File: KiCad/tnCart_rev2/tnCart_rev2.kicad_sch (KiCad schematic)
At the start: 97 parts, among them CN1 MSX_Cartridge, J1 Conn_01x06_Pin, J2 ST-005-G, Q10 2SC2712, Q11 2SC2712, SW1 SW_DIP_x01, U1 TangNano20K, U10 TC74LCX163245FT, U20 TC74LCX163245FT, U30 TC74LCX163245FT, U40 74LVC1G139, U41 74LVC1G125, U60 LP2985-3.3, U70 LMV7219M5, U71 R-R, U80 LMV7219M5, U81 R-R, U90 LMV7219M5, U91 R-R

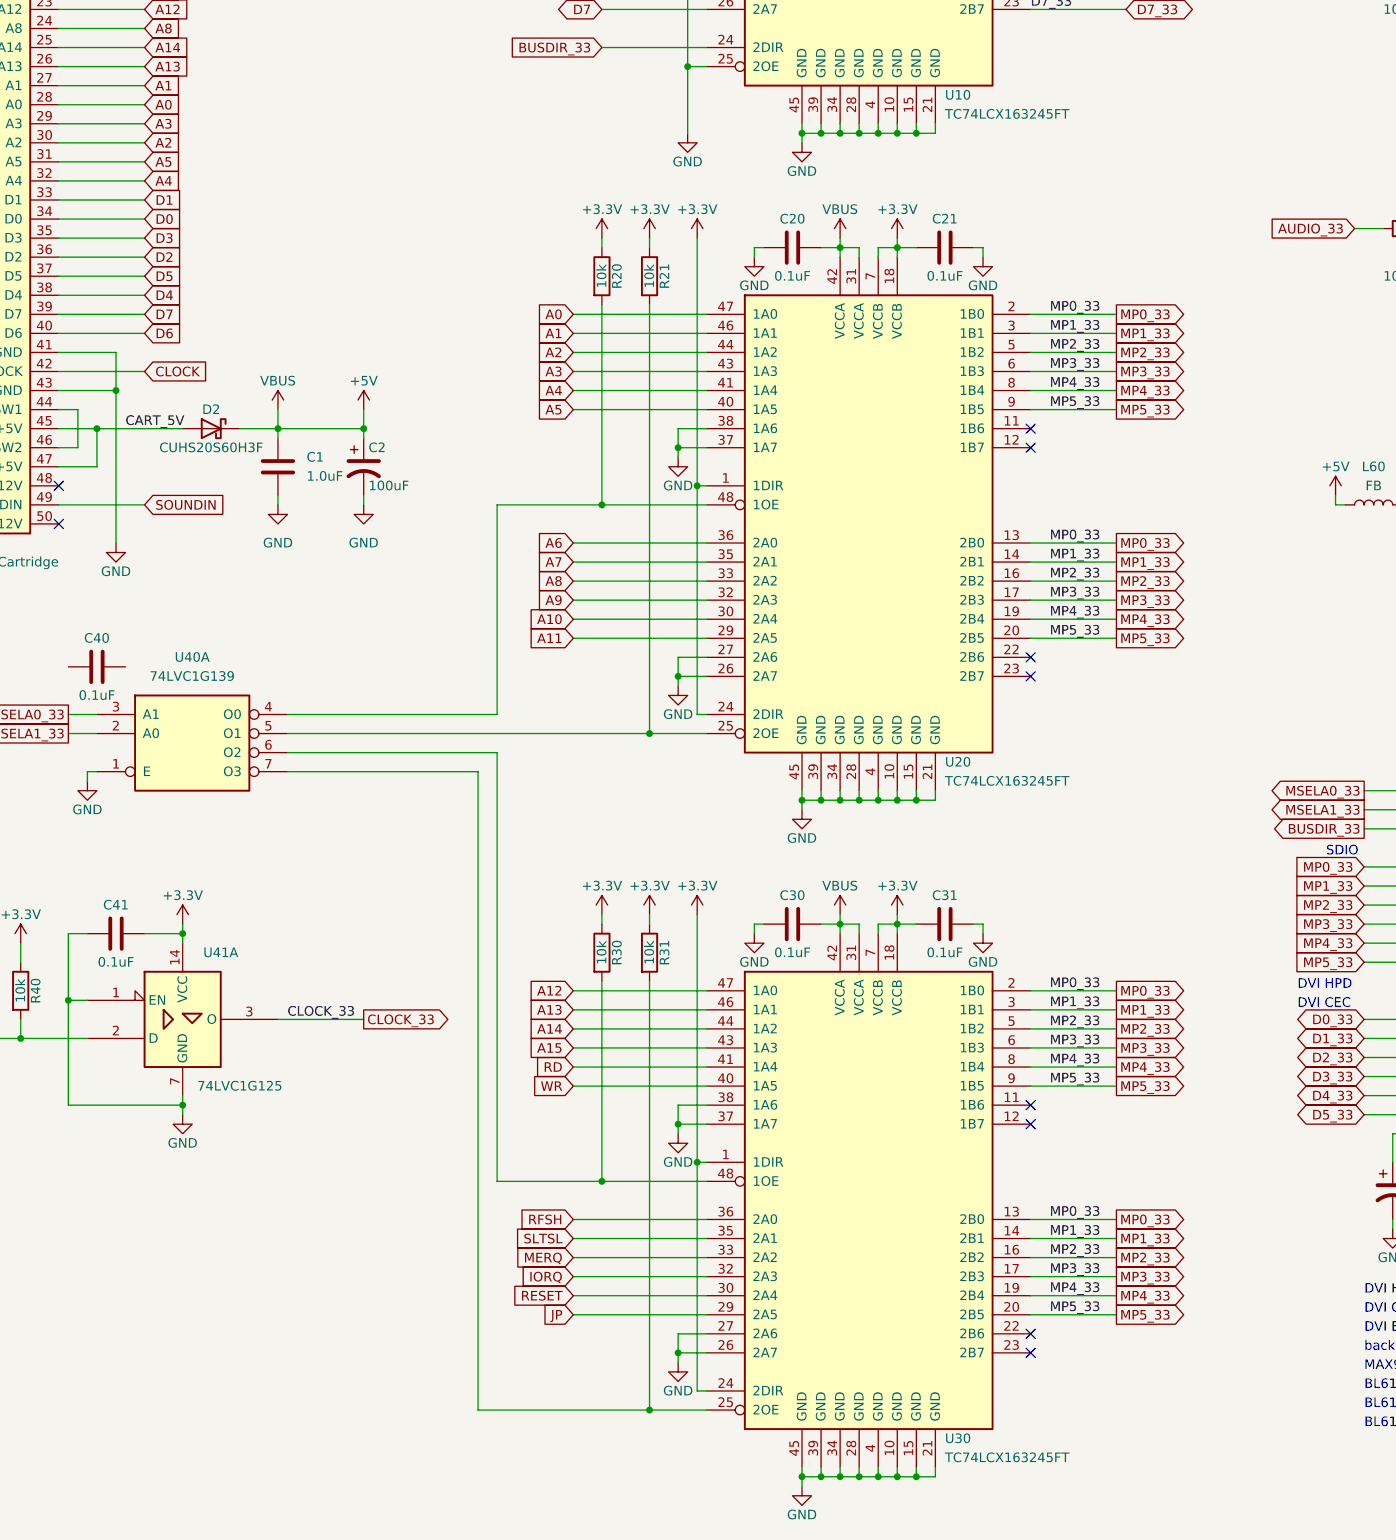
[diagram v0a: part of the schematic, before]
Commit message: Modify MUX operation timing to compensate for rev2 circuit delay.
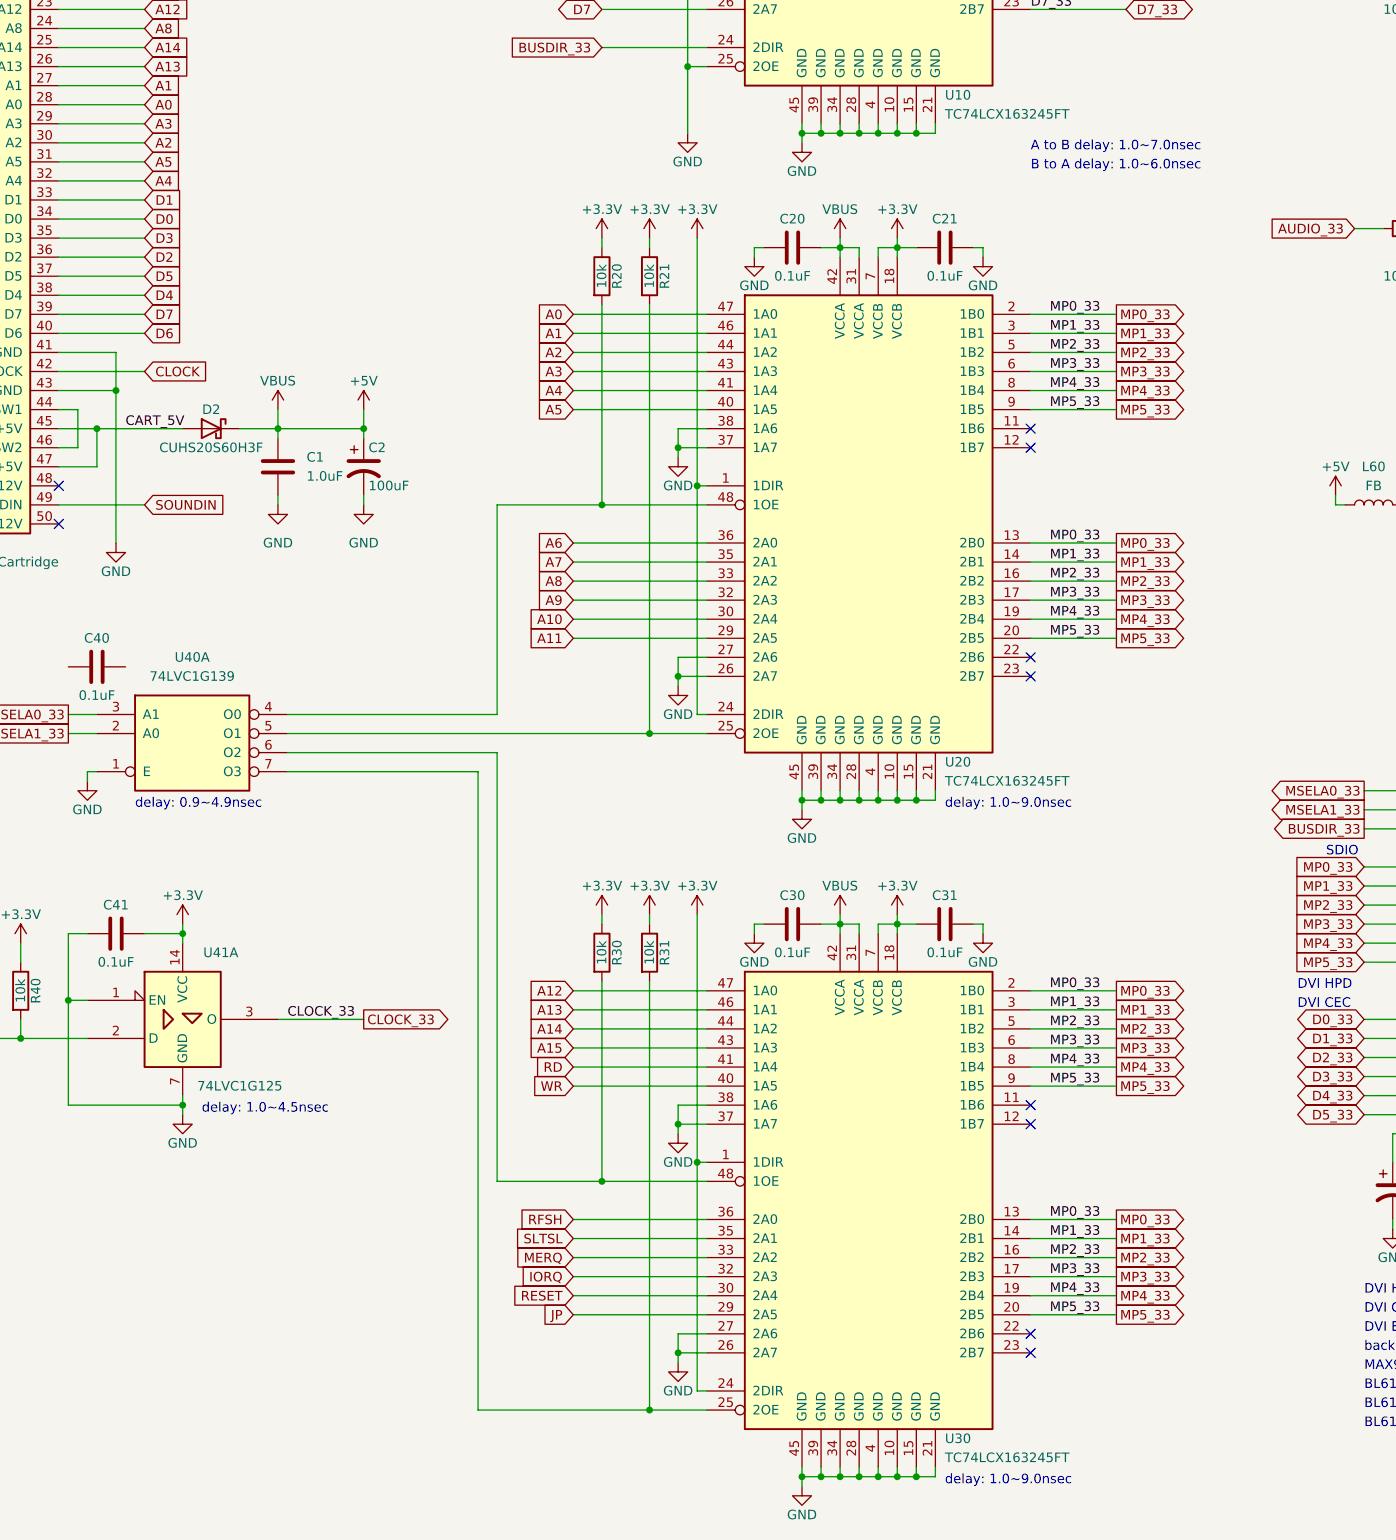
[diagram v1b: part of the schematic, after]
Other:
- note added: "A to B delay: 1.0~7.0nsec"
- note added: "B to A delay: 1.0~6.0nsec"
- note added: "delay: 0.9~4.9nsec"
- note added: "delay: 1.0~4.5nsec"
- note added: "delay: 1.0~9.0nsec"
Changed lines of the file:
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@@
+    (effects (font (size 1.27 1.27)) (justify left bottom))
+  )
+  (text "B to A delay: 1.0~6.0nsec" (at 181.61 99.06 0)
+    (effects (font (size 1.27 1.27)) (justify left bottom))
+  )
+  (text "delay: 0.9~4.9nsec" (at 62.23 184.15 0)
+    (effects (font (size 1.27 1.27)) (justify left bottom))
+  )
+  (text "A to B delay: 1.0~7.0nsec" (at 181.61 96.52 0)
+    (effects (font (size 1.27 1.27)) (justify left bottom))
+  )
+  (text "delay: 1.0~4.5nsec" (at 71.12 224.79 0)
     (effects (font (size 1.27 1.27)) (justify left bottom))
   )
@@
     (effects (font (size 1.27 1.27)) (justify left bottom))
   )
+  (text "delay: 1.0~9.0nsec" (at 170.18 184.15 0)
+    (effects (font (size 1.27 1.27)) (justify left bottom))
+  )
   (text "back light enable" (at 309.88 210.82 0)
     (effects (font (size 1.27 1.27)) (justify left bottom))
   )
+  (text "delay: 1.0~9.0nsec" (at 170.18 274.32 0)
+    (effects (font (size 1.27 1.27)) (justify left bottom))
+  )

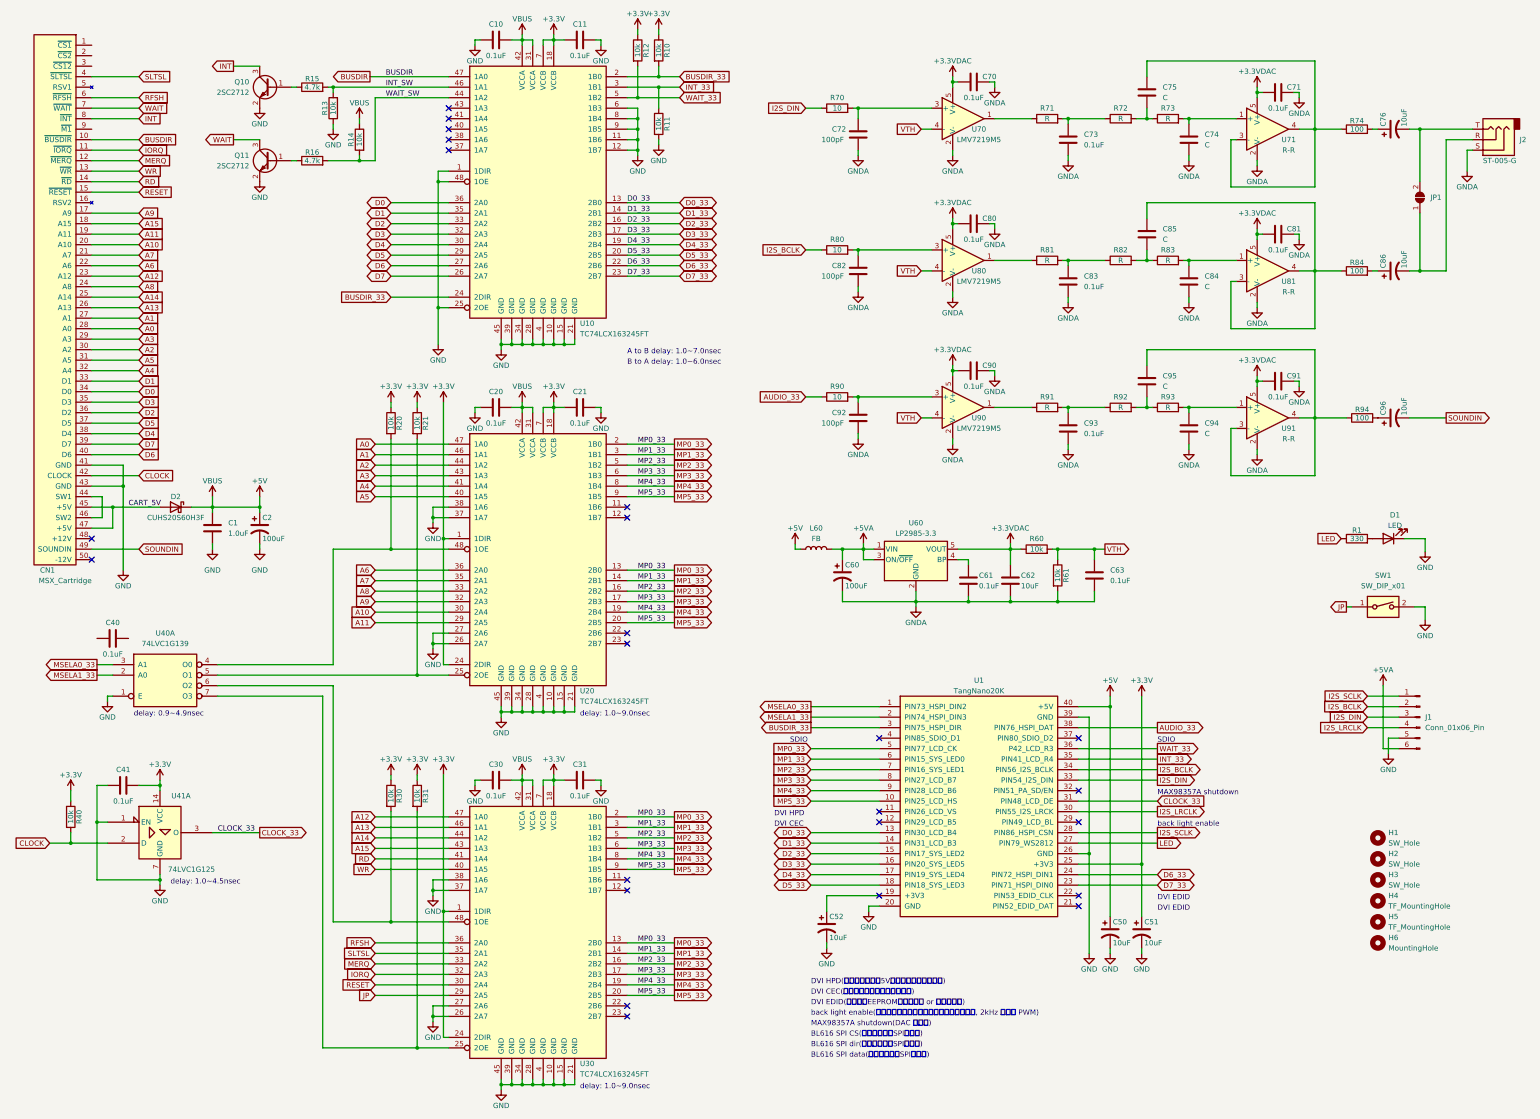
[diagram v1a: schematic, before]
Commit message: modify rev2 schematic
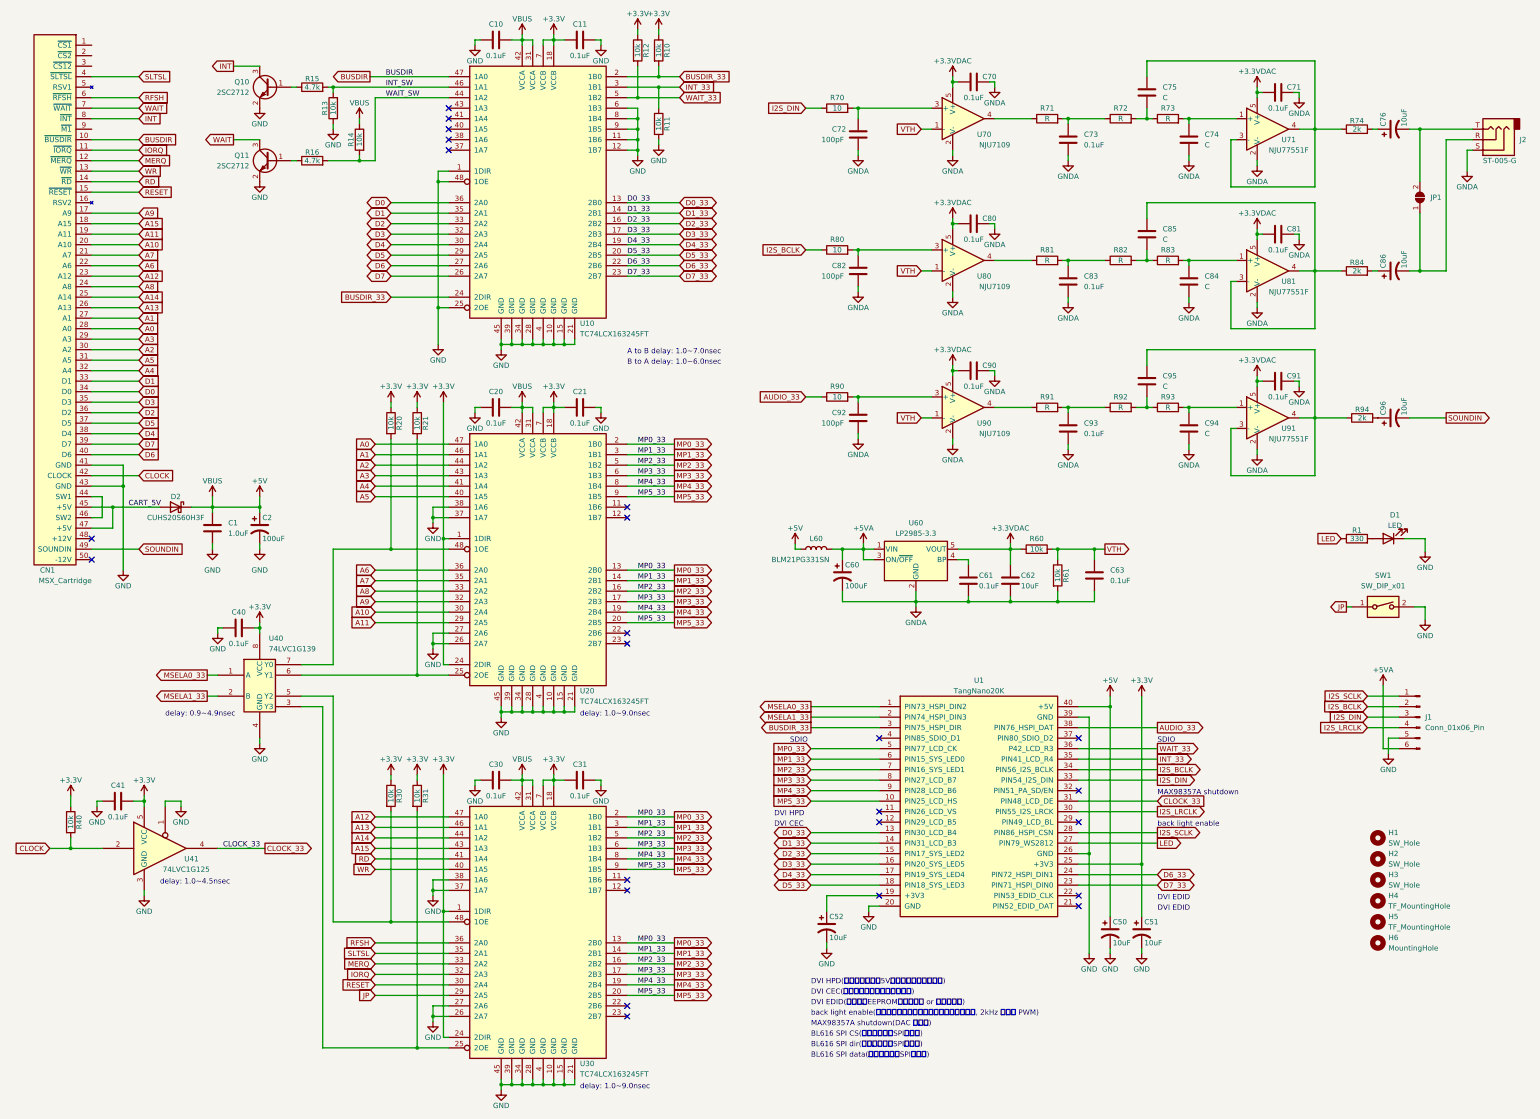
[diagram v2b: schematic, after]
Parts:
- removed U40: 74LVC1G139, symbol 74xx:74LS139
- removed U41: 74LVC1G125, symbol 74xx_IEEE:74125
- removed U70, U80, U90: LMV7219M5, Package_TO_SOT_SMD:SOT-23-5, symbol Comparator:LMV7219M5
- added U40: 74LVC1G139, symbol 74xGxx:74LVC1G139
- added U41: 74LVC1G125, symbol 74xGxx:74LVC1G125
- added U70, U80, U90: NJU7109, symbol mylib:NJU7109
- L60: value FB -> BLM21PG331SN
- R74, R84, R94: value 100 -> 2k
- U71, U81, U91: value R-R -> NJU77551F
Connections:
- net +3.3V: now also C40.2, U40.8 (VCC), U41.5 (VCC)
- net +3.3VDAC: now also U70.5 (V+), U80.5 (V+), U90.5 (V+)
- net CLOCK: now also U41.2
- net CLOCK_33: now also U41.4
- net GND: now also C40.1, U40.4 (GND), U41.1, U41.3 (GND)
- net GNDA: now also U70.2 (V-), U80.2 (V-), U90.2 (V-)
- net MSELA0_33: now also U40.1 (A)
- net MSELA1_33: now also U40.2 (B)
- net VTH: now also U70.1 (-), U80.1 (-), U90.1 (-)
- net at R81.1: now also U80.4
- net at C82.1, R80.2: now also U80.3 (+)
- net at C92.1, R90.2: now also U90.3 (+)
- net at R31.2, U30.25 (2OE): now also U40.3 (Y3)
- net at C72.1, R70.2: now also U70.3 (+)
- net at R71.1: now also U70.4
- net at R91.1: now also U90.4
- net at R30.2, U30.48 (1OE): now also U40.5 (Y2)
- net at R21.2, U20.25 (2OE): now also U40.6 (Y1)
- net at R20.2, U20.48 (1OE): now also U40.7 (Y0)
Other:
- moved on the sheet: C40, C41, R40
